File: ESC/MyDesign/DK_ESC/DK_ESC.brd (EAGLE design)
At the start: 88.9 x 81 mm, 52 parts, among them IC2 7805

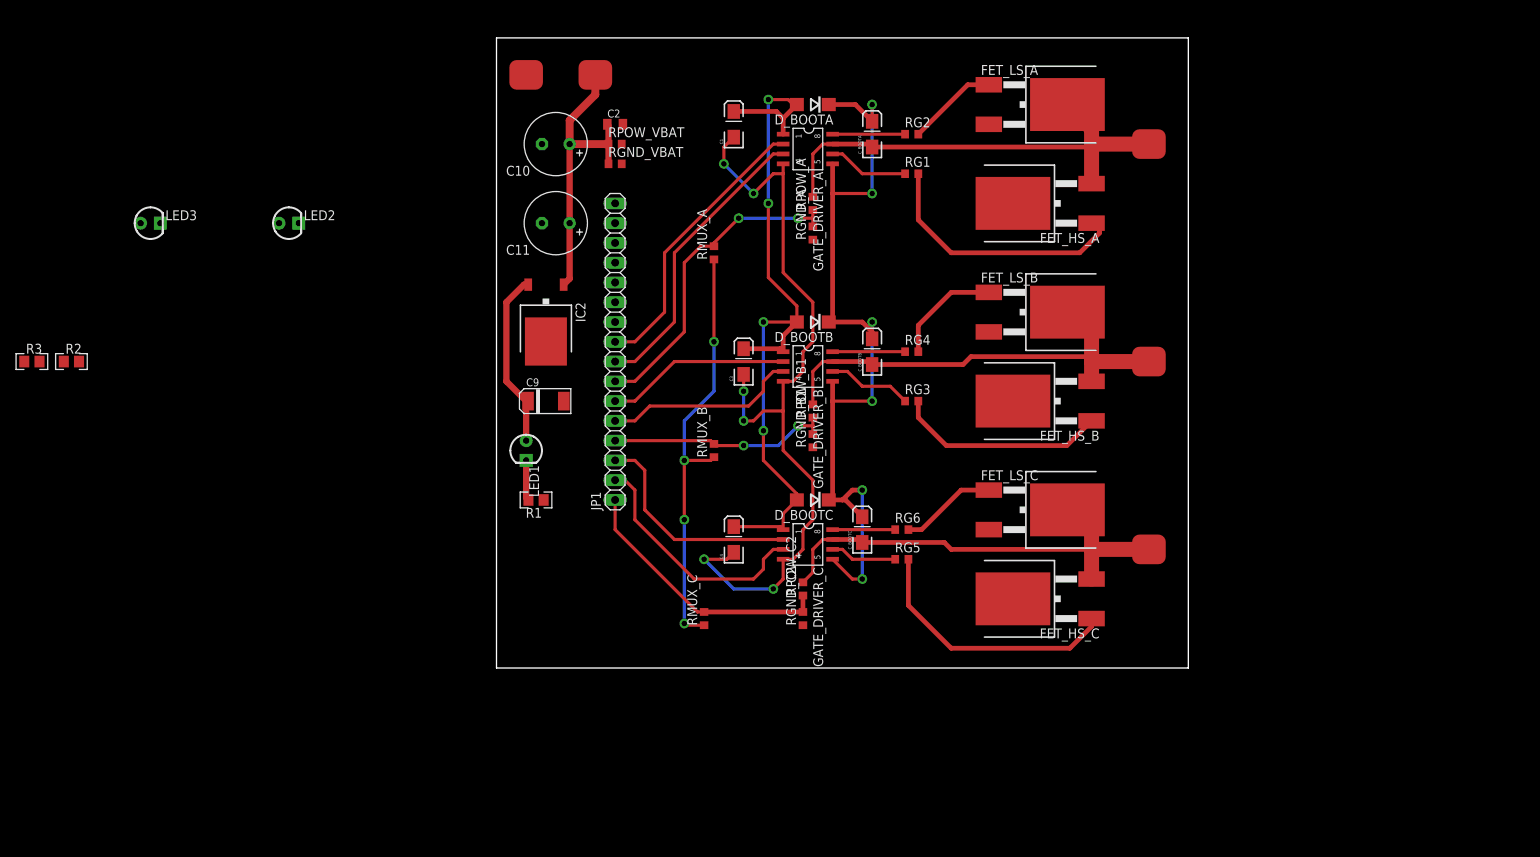
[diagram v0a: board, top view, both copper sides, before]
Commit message: Add Datasheet mosfet and update layout test ESC
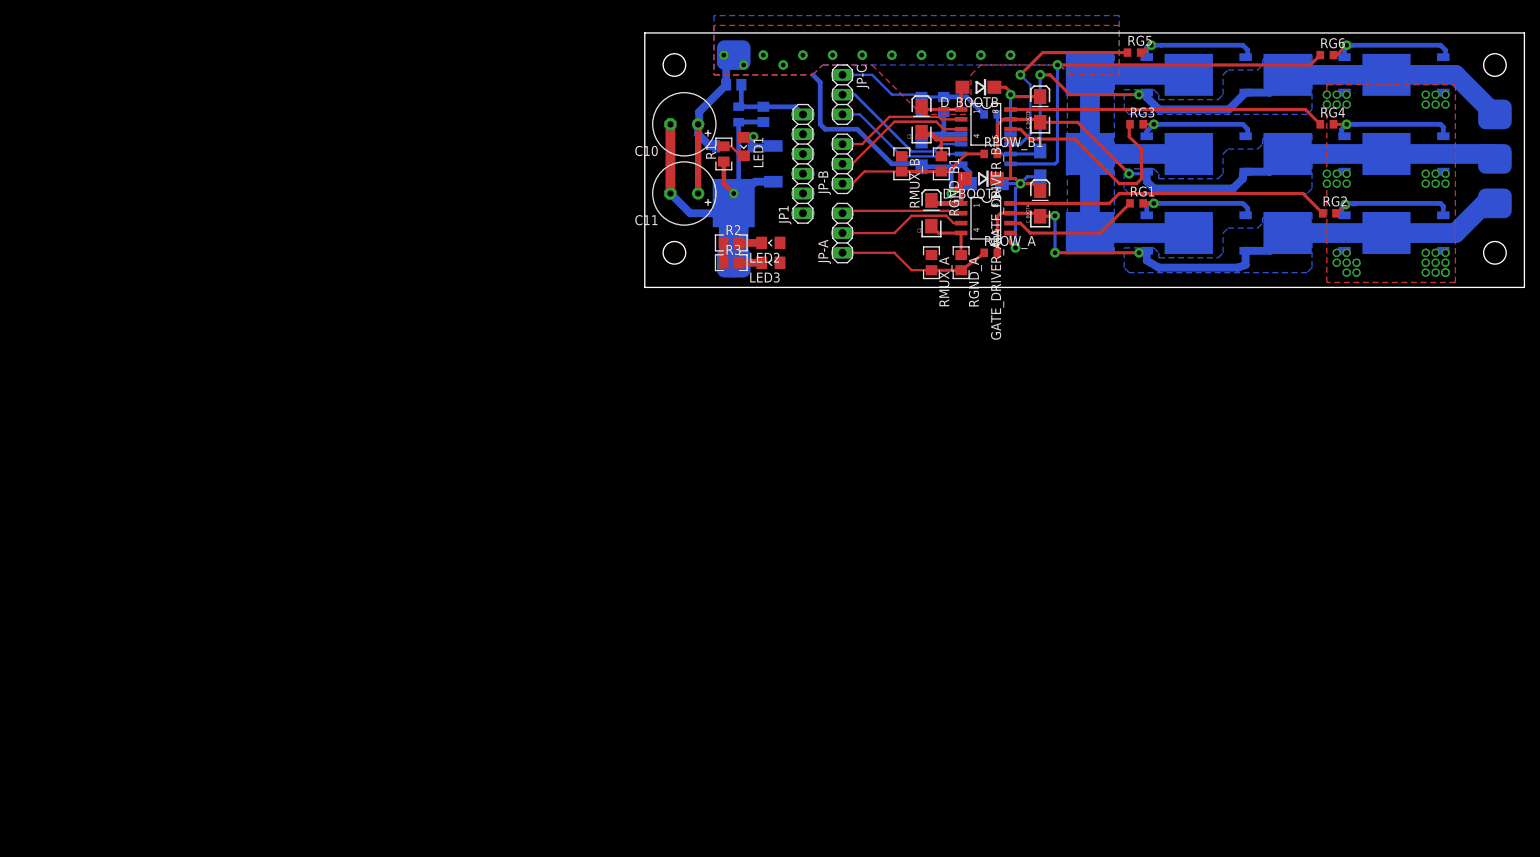
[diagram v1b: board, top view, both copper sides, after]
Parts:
- added FET_HS_A1, FET_HS_B1, FET_HS_C1, FET_LS_A1, FET_LS_B1, FET_LS_C1: IRLR7843TRPBF, FET:TO252
- added JP-A, JP-B, JP-C: (no value), pinhead:1X03
- FET_HS_A, FET_HS_B, FET_HS_C, FET_LS_A, FET_LS_B, FET_LS_C: value IRF3709-TO-263 -> IRLR7843TRPBF; device FET:TO263 -> FET:TO252
- JP1: device pinhead:1X16 -> pinhead:1X06
- LED1, LED2, LED3: device LED:LED3MM -> LED:LED_0805
- RGND_A, RGND_B1, RGND_C2, RMUX_A, RMUX_B, RMUX_C: value 10k -> 10k 1%; device RCL:R0603 -> RCL:R0805
- RGND_VBAT: value 2k 1% -> 1k 1%; device RCL:R0603 -> RCL:R0805
- RPOW_A, RPOW_B1, RPOW_C2: value 47k -> 47k 1%
- RPOW_VBAT: value 47k 1% -> 10k 1%; device RCL:R0603 -> RCL:R0805
- moved R3 90.7 mm to (21.3, 69.8)
- moved R2 86.1 mm to (21.3, 72.4)
- moved RG6 81.8 mm to (97.8, 96.5)
- moved LED3 79.9 mm to (26.4, 69.8), turned to 90 degrees
- moved FET_LS_C 73.0 mm to (108.0, 94.0), flipped to the bottom
- moved RMUX_C 71.7 mm to (45.7, 90.2), flipped to the bottom
- moved RG5 71.6 mm to (73.0, 96.8)
- moved MC 71.4 mm to (119.4, 88.9), flipped to the bottom, turned to 180 degrees
- moved RGND_C2 68.5 mm to (48.6, 90.2), flipped to the bottom
- moved FET_HS_C 67.9 mm to (69.8, 94.0), flipped to the bottom, turned to 270 degrees
- moved RPOW_C2 65.6 mm to (54.6, 88.9), flipped to the bottom, turned to 180 degrees
- moved LED2 62.0 mm to (26.4, 72.4), turned to 90 degrees
- moved RG4 60.8 mm to (97.8, 87.6)
- moved GATE_DRIVER_C 56.9 mm to (53.3, 85.1), flipped to the bottom, turned to 90 degrees
- moved C4 55.1 mm to (45.7, 83.8), flipped to the bottom, turned to 270 degrees
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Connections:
- removed net +12V: C1.A, C3.A, C4.A, D_BOOTA.A, D_BOOTB.A, D_BOOTC.A, GATE_DRIVER_A.1, GATE_DRIVER_B.1, GATE_DRIVER_C.1
- removed net COM: C1.C, C3.C, C4.C, GATE_DRIVER_A.4, GATE_DRIVER_B.4, GATE_DRIVER_C.4
- removed net N$14: JP1.16
- removed net N$15: JP1.15
- removed net N$18: JP1.14
- removed net N$19: JP1.13
- removed net N$20: JP1.12
- removed net N$21: JP1.11
- removed net N$22: JP1.10
- net A_MOTOR: now also FET_HS_A1.3, FET_LS_A1.2
- net B_MOTOR: now also FET_HS_B1.3, FET_LS_B1.2
- net C_MOTOR: now also FET_HS_C1.3, FET_LS_C1.2
- net GND: now also C1.C, C3.C, C4.C, FET_LS_A1.3, FET_LS_B1.3, FET_LS_C1.3, GATE_DRIVER_A.4, GATE_DRIVER_B.4, GATE_DRIVER_C.4
- net HS_A: now also JP-A.3; no longer JP1.9
- net HS_B: now also JP-B.3; no longer JP1.6
- net HS_C: now also JP-C.3; no longer JP1.3
- net LS_A: now also JP-A.2; no longer JP1.8
- net LS_B: now also JP-B.2; no longer JP1.5
- net LS_C: now also JP-C.2; no longer JP1.2
- net MUX_A_EMF: now also JP-A.1; no longer JP1.7
- net MUX_B_EMF: now also JP-B.1; no longer JP1.4
- net MUX_C_EMF: now also JP-C.1; no longer JP1.1
- net MUX_VBAT: now also JP1.6
- net N$1: now also FET_LS_A1.1
- net N$10: now also FET_HS_C1.1
- net N$13: now also LED1.C; no longer LED1.K
- net N$16: now also LED2.C; no longer LED2.K
- net N$17: now also LED3.C; no longer LED3.K
- net N$2: now also FET_HS_A1.1
- net N$3: now also FET_LS_B1.1
- net N$6: now also FET_HS_B1.1
- net N$9: now also FET_LS_C1.1
- net VDD: now also C1.A, C3.A, C4.A, D_BOOTA.A, D_BOOTB.A, D_BOOTC.A, FET_HS_A1.2, FET_HS_B1.2, FET_HS_C1.2, GATE_DRIVER_A.1, GATE_DRIVER_B.1, GATE_DRIVER_C.1
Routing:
- net COM: track 103.4 -> 0.00 mm, vias 6 -> 0
- net VDD: track 33.2 -> 136.5 mm, vias 0 -> 13
- net +12V: track 95.0 -> 0.00 mm, vias 4 -> 0
- net GND: track 0.00 -> 76.6 mm, vias 0 -> 42
- net VB: track 109.6 -> 38.9 mm, vias 6 -> 3
- net COMMON_COMPARATOR: track 55.0 -> 0.00 mm, vias 4 -> 0
- net N$12: track 8.04 -> 52.8 mm, vias 0 -> 1
- net N$5: track 9.31 -> 41.7 mm
- net N$8: track 9.31 -> 40.6 mm
- net MUX_A_EMF: track 41.6 -> 19.9 mm, vias 2 -> 0
- net LS_A: track 37.8 -> 16.6 mm
- net HS_A: track 36.6 -> 15.5 mm
- net C_MOTOR: track 65.0 -> 85.8 mm, vias 0 -> 2
- net A_MOTOR: track 61.0 -> 79.7 mm, vias 0 -> 3
- net N$11: track 8.57 -> 26.2 mm, vias 0 -> 1
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- added copper zone on layer 16, net A_MOTOR
- added copper zone on layer 16, net B_MOTOR
- added copper zone on layer 16, net C_MOTOR
- added copper zone on layer 1, net GND
- added copper zone on layer 1, net VDD
- added copper zone on layer 16, net VDD
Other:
- board size 88.9 x 81 mm -> 113 x 32.7 mm

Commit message: Finish layout test ESC
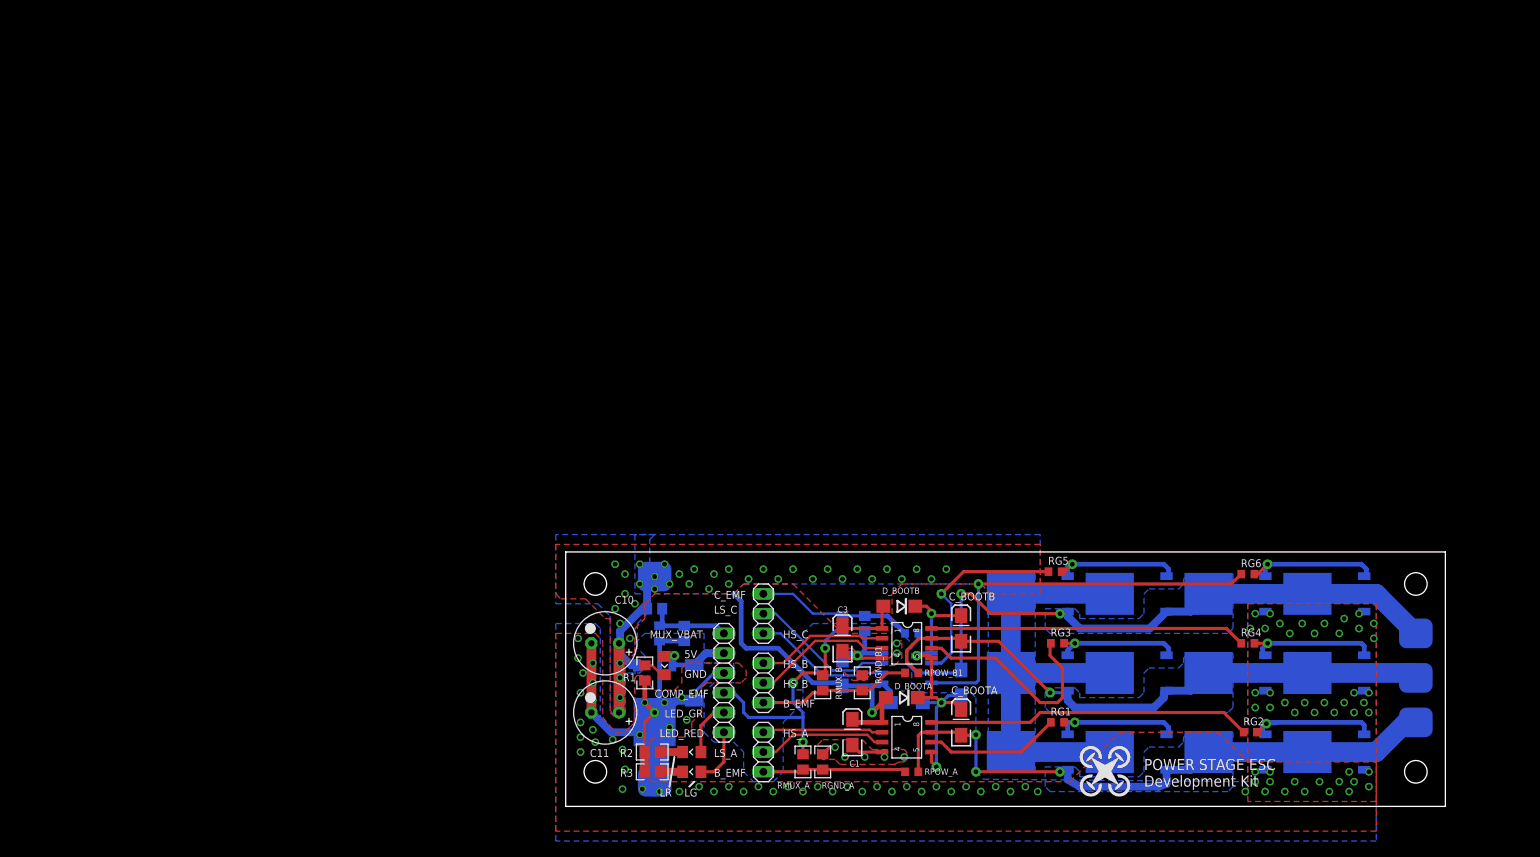
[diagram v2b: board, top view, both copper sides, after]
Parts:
- added U$2: QUADCOPTER-MEDIUM, logo:QUADCOPTER-250MIL
- moved RPOW_VBAT 68.1 mm to (11.4, 25.4)
- moved BAT+ 67.8 mm to (11.4, 29.5)
- moved C2 67.4 mm to (12.1, 22.2)
- moved D_BOOTC 67.4 mm to (43.8, 13.3)
- moved FET_HS_C 67.4 mm to (59.7, 27.3)
- moved FET_HS_C1 67.4 mm to (72.4, 27.3)
- moved FET_LS_C 67.4 mm to (97.8, 27.3)
- moved FET_LS_C1 67.4 mm to (85.1, 27.3)
- moved GATE_DRIVER_A 67.4 mm to (43.2, 8.26)
- moved GATE_DRIVER_B 67.4 mm to (43.2, 20.3)
- moved GATE_DRIVER_C 67.4 mm to (43.2, 18.4)
- moved IC2 67.4 mm to (11.4, 13.3)
- moved MC 67.4 mm to (109.2, 22.2)
- moved RG5 67.4 mm to (62.9, 30.2)
- moved RGND_VBAT 67.4 mm to (15.2, 22.2)
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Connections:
- net +5V: now also JP1.5
- net COMMON_COMPARATOR: now also JP1.3
- net GND: now also JP1.4
- net LED_GREEN: now also JP1.2
- net LED_RED: now also JP1.1
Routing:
- net COMMON_COMPARATOR: track 0.00 -> 33.7 mm, vias 0 -> 3
- net GND: track 76.6 -> 91.5 mm, vias 42 -> 107
- net LS_C: track 29.0 -> 18.7 mm
- net LED_RED: track 0.00 -> 7.29 mm
- net LED_GREEN: track 0.00 -> 7.05 mm
- net LS_B: track 23.3 -> 17.9 mm
- net +5V: track 5.45 -> 9.88 mm
- net VB: track 38.9 -> 43.0 mm, vias 3 -> 4
- net B_MOTOR: track 75.0 -> 76.6 mm
- net C_MOTOR: track 85.8 -> 87.4 mm
- net VDD: track 136.5 -> 137.9 mm, vias 13 -> 38
- net MUX_A_EMF: track 19.9 -> 18.9 mm
- net MUX_VBAT: track 11.6 -> 11.0 mm
- added copper zone on layer 16, net GND
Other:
- board text added: "+"
- board text added: "-"
- board text added: "5V"
- board text added: "A"
- board text added: "B"
- board text added: "B_EMF"
- board text added: "C"
- board text added: "COMP_EMF"
- board text added: "C_EMF"
- board text added: "D_BOOTB"
- board text added: "GND"
- board text added: "HS_A"
- board text added: "HS_B"
- board text added: "HS_C"
- board text added: "LED_GR"
- board text added: "LED_RED"
- board text added: "LG"
- board text added: "LR"
- board text added: "LS_A"
- board text added: "LS_C"
- board text added: "MUX_VBAT"
- board text added: "POWER STAGE ESC Development Kit"
- board text added: "R2"
- board text added: "R3"

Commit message: Update logo renesas
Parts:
- U$2: value QUADCOPTER-MEDIUM -> RENESAS; device logo:QUADCOPTER-250MIL -> logo:RENESAS
- moved U$2 3.55 mm to (66.7, 4.76)
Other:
- board text added: "Design by KietDD"
- board text added: "RH950 Family (Flying Car only) Development Kit"
- board text removed: "POWER STAGE ESC Development Kit"
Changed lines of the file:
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@@
 <text x="6.985" y="6.35" size="1.016" layer="25" font="vector" ratio="12">R2</text>
 <text x="19.05" y="26.67" size="1.016" layer="25" font="vector" ratio="12">C_EMF</text>
-<text x="19.05" y="24.765" size="1.016" layer="25" font="vector" ratio="12">LS_C</text>
+<text x="19.05" y="24.13" size="1.016" layer="25" font="vector" ratio="12">LS_C</text>
 <text x="27.94" y="21.59" size="1.016" layer="25" font="vector" ratio="12">HS_C</text>
 <text x="27.94" y="17.78" size="1.016" layer="25" font="vector" ratio="12">HS_B</text>
@@
 <text x="106.045" y="15.24" size="2.54" layer="26" font="vector" ratio="12" rot="MR0">B</text>
 <text x="106.045" y="10.16" size="2.54" layer="26" font="vector" ratio="12" rot="MR0">A</text>
-<circle x="3.175" y="22.86" radius="0.70995" width="0" layer="25"/>
-<circle x="3.175" y="13.97" radius="0.70995" width="0" layer="25"/>
-<text x="74.295" y="2.54" size="1.4224" layer="25" font="vector" ratio="12">POWER STAGE ESC
+<circle x="3.175" y="19.05" radius="0.70995" width="0" layer="25"/>
+<circle x="3.175" y="10.16" radius="0.70995" width="0" layer="25"/>
+<text x="66.675" y="0.9525" size="1.524" layer="25" ratio="12">RH950 Family (Flying Car only)
 Development Kit</text>
+<text x="10.16" y="30.48" size="1.016" layer="25" ratio="12">Design by KietDD</text>
 </plain>
 <attributes>
@@
 <attribute name="VALUE" x="23.495" y="8.255" size="1.27" layer="27" rot="R90"/>
 </element>
-<element name="U$2" library="logo" package="QUADCOPTER-250MIL" value="QUADCOPTER-MEDIUM" x="66.04" y="1.27"/>
+<element name="U$2" library="logo" package="RENESAS" value="RENESAS" x="66.675" y="4.7625"/>
 </elements>
 <signals>
